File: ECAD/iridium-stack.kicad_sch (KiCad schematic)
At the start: 10 parts

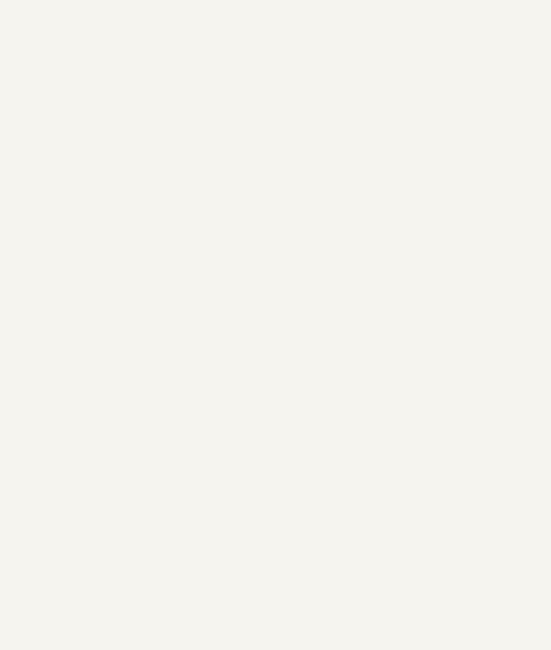
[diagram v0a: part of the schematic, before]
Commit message: finish symbol, update footprint
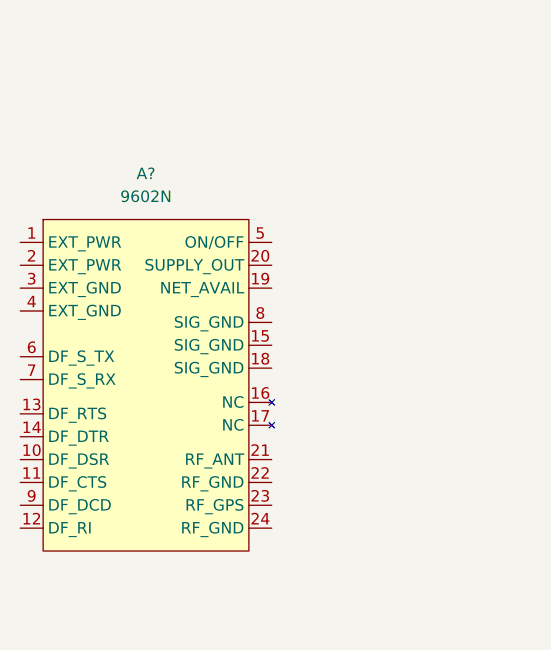
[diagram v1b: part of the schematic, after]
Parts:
- added A?: 9602N, symbol 9602N:9602N
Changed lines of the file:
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@@
     (pin "1")
+  )
+  (symbol (lib_id "9602N:9602N") (at 133.35 64.77 0) (unit 1)
+    (in_bom yes) (on_board yes) (fields_autoplaced)
+    (property "Reference" "A?" (id 0) (at 133.35 60.96 0))
+    (property "Value" "9602N" (id 1) (at 133.35 63.5 0))
+    (property "Footprint" "" (id 2) (at 133.35 64.77 0)
+      (effects (font (size 1.27 1.27)) hide)
+    )
+    (property "Datasheet" "" (id 3) (at 133.35 64.77 0)
+      (effects (font (size 1.27 1.27)) hide)
+    )
+    (pin "1")
+    (pin "10")
+    (pin "11")
+    (pin "12")
+    (pin "13")
+    (pin "14")
+    (pin "15")
+    (pin "16")
+    (pin "17")
+    (pin "18")
+    (pin "19")
+    (pin "2")
+    (pin "20")
+    (pin "21")
+    (pin "22")
+    (pin "23")
+    (pin "24")
+    (pin "3")
+    (pin "4")
+    (pin "5")
+    (pin "6")
+    (pin "7")
+    (pin "8")
+    (pin "9")
   )
   (sheet_instances
@@
       (reference "#PWR0112") (unit 1) (value "GND") (footprint "")
     )
+    (path "/4d3f3d34-821b-4ab9-8d48-8bbca7e30590"
+      (reference "A?") (unit 1) (value "9602N") (footprint "")
+    )
     (path "/00000000-0000-0000-0000-0000622296c8"

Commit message: power
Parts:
- added TH?: NTC, symbol Device:Thermistor_NTC
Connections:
- net +5V: now also TH?.2
- net GND: now also A?.3 (EXT_GND), A?.4 (EXT_GND)
- net +5VP: now reaches A?.1 (EXT_PWR)
- net +5VP: now also A?.2 (EXT_PWR), TH?.1
- net at A?.15 (SIG_GND): now also A?.18 (SIG_GND), A?.8 (SIG_GND)
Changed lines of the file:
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@@
   (junction (at 270.51 85.09) (diameter 0) (color 0 0 0 0)
   )
+  (junction (at 116.84 68.58) (diameter 0) (color 0 0 0 0)
+  )
+  (junction (at 116.84 76.2) (diameter 0) (color 0 0 0 0)
+  )
+  (junction (at 149.86 80.01) (diameter 0) (color 0 0 0 0)
+  )
+  (wire (pts (xy 147.32 77.47) (xy 149.86 77.47))
+    (stroke (width 0) (type default) (color 0 0 0 0))
+  )
   (wire (pts (xy 250.19 82.55) (xy 254 82.55))
     (stroke (width 0) (type default) (color 0 0 0 0))
   )
+  (wire (pts (xy 93.98 54.61) (xy 97.79 54.61))
+    (stroke (width 0) (type default) (color 0 0 0 0))
+  )
+  (wire (pts (xy 149.86 77.47) (xy 149.86 80.01))
+    (stroke (width 0) (type default) (color 0 0 0 0))
+  )
+  (wire (pts (xy 116.84 71.12) (xy 119.38 71.12))
+    (stroke (width 0) (type default) (color 0 0 0 0))
+  )
+  (wire (pts (xy 149.86 80.01) (xy 149.86 82.55))
+    (stroke (width 0) (type default) (color 0 0 0 0))
+  )
+  (wire (pts (xy 116.84 68.58) (xy 119.38 68.58))
+    (stroke (width 0) (type default) (color 0 0 0 0))
+  )
   (wire (pts (xy 270.51 85.09) (xy 266.7 85.09))
     (stroke (width 0) (type default) (color 0 0 0 0))
@@
     (stroke (width 0) (type default) (color 0 0 0 0))
   )
+  (wire (pts (xy 119.38 73.66) (xy 116.84 73.66))
+    (stroke (width 0) (type default) (color 0 0 0 0))
+  )
+  (wire (pts (xy 147.32 80.01) (xy 149.86 80.01))
+    (stroke (width 0) (type default) (color 0 0 0 0))
+  )
   (wire (pts (xy 266.7 82.55) (xy 270.51 82.55))
+    (stroke (width 0) (type default) (color 0 0 0 0))
+  )
+  (wire (pts (xy 116.84 68.58) (xy 116.84 71.12))
+    (stroke (width 0) (type default) (color 0 0 0 0))
+  )
+  (wire (pts (xy 116.84 73.66) (xy 116.84 76.2))
+    (stroke (width 0) (type default) (color 0 0 0 0))
+  )
+  (wire (pts (xy 149.86 82.55) (xy 147.32 82.55))
+    (stroke (width 0) (type default) (color 0 0 0 0))
+  )
+  (wire (pts (xy 116.84 76.2) (xy 119.38 76.2))
+    (stroke (width 0) (type default) (color 0 0 0 0))
+  )
+  (wire (pts (xy 82.55 54.61) (xy 86.36 54.61))
     (stroke (width 0) (type default) (color 0 0 0 0))
   )
@@
     (pin "1")
   )
+  (symbol (lib_id "power:GND") (at 116.84 76.2 0) (unit 1)
+    (in_bom yes) (on_board yes)
+    (property "Reference" "#PWR?" (id 0) (at 116.84 82.55 0)
+      (effects (font (size 1.27 1.27)) hide)
+    )
+    (property "Value" "GND" (id 1) (at 116.84 80.01 0))
+    (property "Footprint" "" (id 2) (at 116.84 76.2 0)
+      (effects (font (size 1.27 1.27)) hide)
+    )
+    (property "Datasheet" "" (id 3) (at 116.84 76.2 0)
+      (effects (font (size 1.27 1.27)) hide)
+    )
+    (pin "1")
+  )
   (symbol (lib_id "9602N:9602N") (at 133.35 64.77 0) (unit 1)
     (in_bom yes) (on_board yes) (fields_autoplaced)
@@
     (pin "9")
   )
+  (symbol (lib_id "Device:Thermistor_NTC") (at 90.17 54.61 270) (unit 1)
+    (in_bom yes) (on_board yes)
+    (property "Reference" "TH?" (id 0) (at 90.17 48.26 90))
+    (property "Value" "NTC" (id 1) (at 90.17 50.8 90))
+    (property "Footprint" "" (id 2) (at 91.44 54.61 0)
+      (effects (font (size 1.27 1.27)) hide)
+    )
+    (property "Datasheet" "~" (id 3) (at 91.44 54.61 0)
+      (effects (font (size 1.27 1.27)) hide)
+    )
+    (pin "1")
+    (pin "2")
+  )
+  (symbol (lib_id "power:+5VP") (at 116.84 68.58 0) (unit 1)
+    (in_bom yes) (on_board yes) (fields_autoplaced)
+    (property "Reference" "#PWR?" (id 0) (at 116.84 72.39 0)
+      (effects (font (size 1.27 1.27)) hide)
+    )
+    (property "Value" "+5VP" (id 1) (at 116.84 63.5 0))
+    (property "Footprint" "" (id 2) (at 116.84 68.58 0)
+      (effects (font (size 1.27 1.27)) hide)
+    )
+    (property "Datasheet" "" (id 3) (at 116.84 68.58 0)
+      (effects (font (size 1.27 1.27)) hide)
+    )
+    (pin "1")
+  )
+  (symbol (lib_id "power:+5V") (at 82.55 54.61 0) (unit 1)
+    (in_bom yes) (on_board yes) (fields_autoplaced)
+    (property "Reference" "#PWR?" (id 0) (at 82.55 58.42 0)
+      (effects (font (size 1.27 1.27)) hide)
+    )
+    (property "Value" "+5V" (id 1) (at 82.55 49.53 0))
+    (property "Footprint" "" (id 2) (at 82.55 54.61 0)
+      (effects (font (size 1.27 1.27)) hide)
+    )
+    (property "Datasheet" "" (id 3) (at 82.55 54.61 0)
+      (effects (font (size 1.27 1.27)) hide)
+    )
+    (pin "1")
+  )
+  (symbol (lib_id "power:+5VP") (at 97.79 54.61 0) (unit 1)
+    (in_bom yes) (on_board yes) (fields_autoplaced)
+    (property "Reference" "#PWR?" (id 0) (at 97.79 58.42 0)
+      (effects (font (size 1.27 1.27)) hide)
+    )
+    (property "Value" "+5VP" (id 1) (at 97.79 49.53 0))
+    (property "Footprint" "" (id 2) (at 97.79 54.61 0)
+      (effects (font (size 1.27 1.27)) hide)
+    )
+    (property "Datasheet" "" (id 3) (at 97.79 54.61 0)
+      (effects (font (size 1.27 1.27)) hide)
+    )
+    (pin "1")
+  )
   (sheet_instances
     (path "/" (page "1"))
@@
       (reference "#PWR0112") (unit 1) (value "GND") (footprint "")
     )
+    (path "/243ec770-cc5a-4509-9c36-eb8c7bb8645d"
+      (reference "#PWR?") (unit 1) (value "GND") (footprint "")
+    )
+    (path "/bf8825e1-0059-4b49-b8f9-cbb3bb661ba2"
+      (reference "#PWR?") (unit 1) (value "+5VP") (footprint "")
+    )
+    (path "/dd479a80-227b-44d6-b0fa-58cd4309c382"
+      (reference "#PWR?") (unit 1) (value "+5V") (footprint "")
+    )
+    (path "/e45ee289-0e09-4fb1-8e60-b9936eece8bf"
+      (reference "#PWR?") (unit 1) (value "+5VP") (footprint "")
+    )
     (path "/4d3f3d34-821b-4ab9-8d48-8bbca7e30590"
       (reference "A?") (unit 1) (value "9602N") (footprint "")
@@
       (reference "MH4") (unit 1) (value "M3") (footprint "MountingHole:MountingHole_3.2mm_M3_Pad")
     )
-  )
+    (path "/b31ebd25-cf4c-4c3e-b83d-0ec793b65cd9"
+      (reference "TH?") (unit 1) (value "NTC") (footprint "")
+    )
+  )

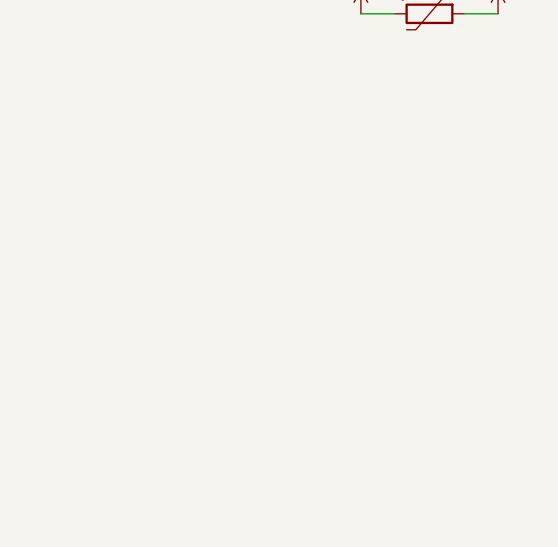
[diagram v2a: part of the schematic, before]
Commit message: add synchronous buck
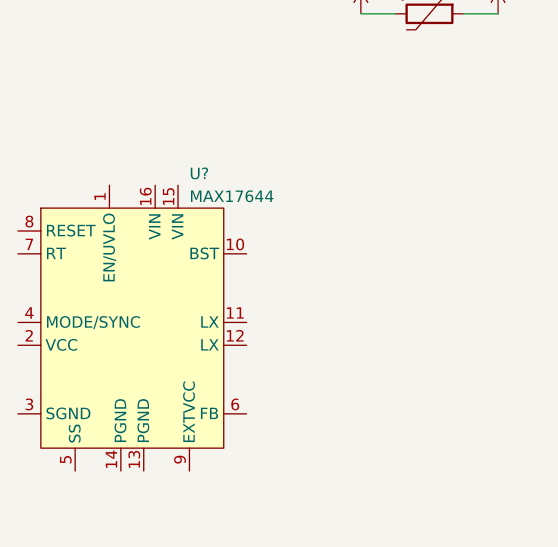
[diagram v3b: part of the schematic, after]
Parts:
- added U?: MAX17644, symbol Symbols:MAX17644
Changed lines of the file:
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@@
     (pin "1")
+  )
+  (symbol (lib_id "Symbols:MAX17644") (at 57.15 71.12 0) (unit 1)
+    (in_bom yes) (on_board yes)
+    (property "Reference" "U?" (id 0) (at 63.5 72.39 0)
+      (effects (font (size 1.27 1.27)) (justify left))
+    )
+    (property "Value" "MAX17644" (id 1) (at 63.5 74.93 0)
+      (effects (font (size 1.27 1.27)) (justify left))
+    )
+    (property "Footprint" "" (id 2) (at 57.15 71.12 0)
+      (effects (font (size 1.27 1.27)) hide)
+    )
+    (property "Datasheet" "" (id 3) (at 57.15 71.12 0)
+      (effects (font (size 1.27 1.27)) hide)
+    )
+    (pin "1")
+    (pin "10")
+    (pin "11")
+    (pin "12")
+    (pin "13")
+    (pin "14")
+    (pin "15")
+    (pin "16")
+    (pin "2")
+    (pin "3")
+    (pin "4")
+    (pin "5")
+    (pin "6")
+    (pin "7")
+    (pin "8")
+    (pin "9")
   )
   (symbol (lib_id "power:GND") (at 116.84 76.2 0) (unit 1)
@@
       (reference "TH?") (unit 1) (value "NTC") (footprint "")
     )
-  )
+    (path "/02a9969f-ce81-4a97-8ae7-0a755196af14"
+      (reference "U?") (unit 1) (value "MAX17644") (footprint "")
+    )
+  )

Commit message: ap62301
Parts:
- removed U?: MAX17644, symbol Symbols:MAX17644
- added C?: 0.1uF, symbol Device:C
- added C?: C, symbol Device:C
- added L?: L, symbol Device:L
- added R? (x2): R, symbol Device:R
- added R?: 3K, symbol Device:R
- added R?: 12.5K, symbol Device:R
- added U?: AP62301WU-7, symbol Symbols:AP62301WU-7
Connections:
- new net: R?.1, R?.2, U?.6 (FB)
- new net: C?.2, R?.2, R?.2, U?.3 (GND)
- new net: C?.1, U?.4 (BST)
- new net: C?.2, L?.1, U?.2 (SW)
- new net: C?.1, R?.1, U?.1 (VIN)
- new net: R?.1, R?.2, U?.5 (EN)
- new net: L?.2, R?.1
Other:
- note added: "6.2V UVLO"
- note added: "Synchronous Buck - Stable 5V"

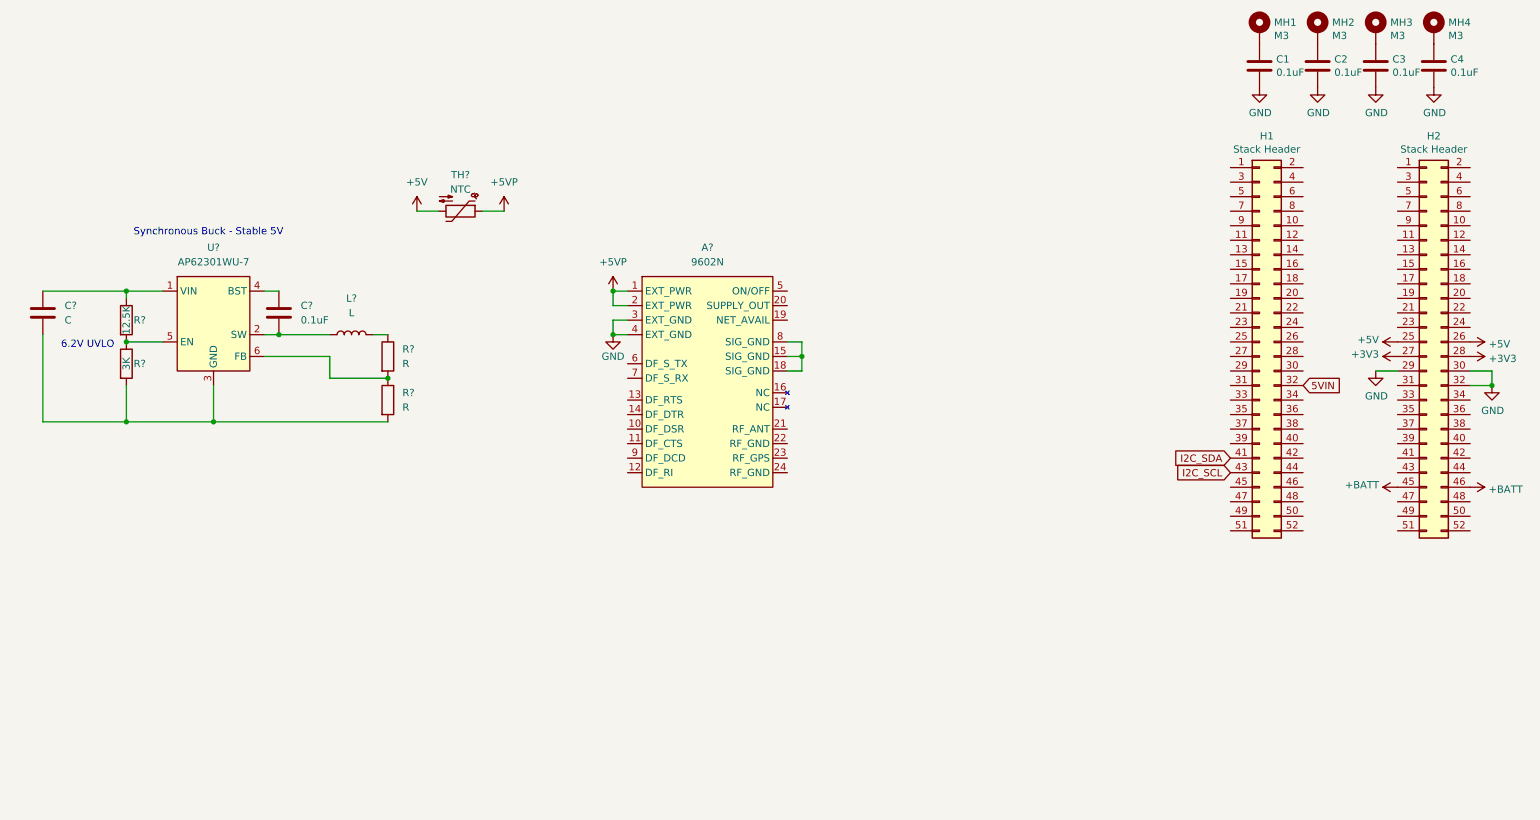
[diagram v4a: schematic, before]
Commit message: Add buck and more nets
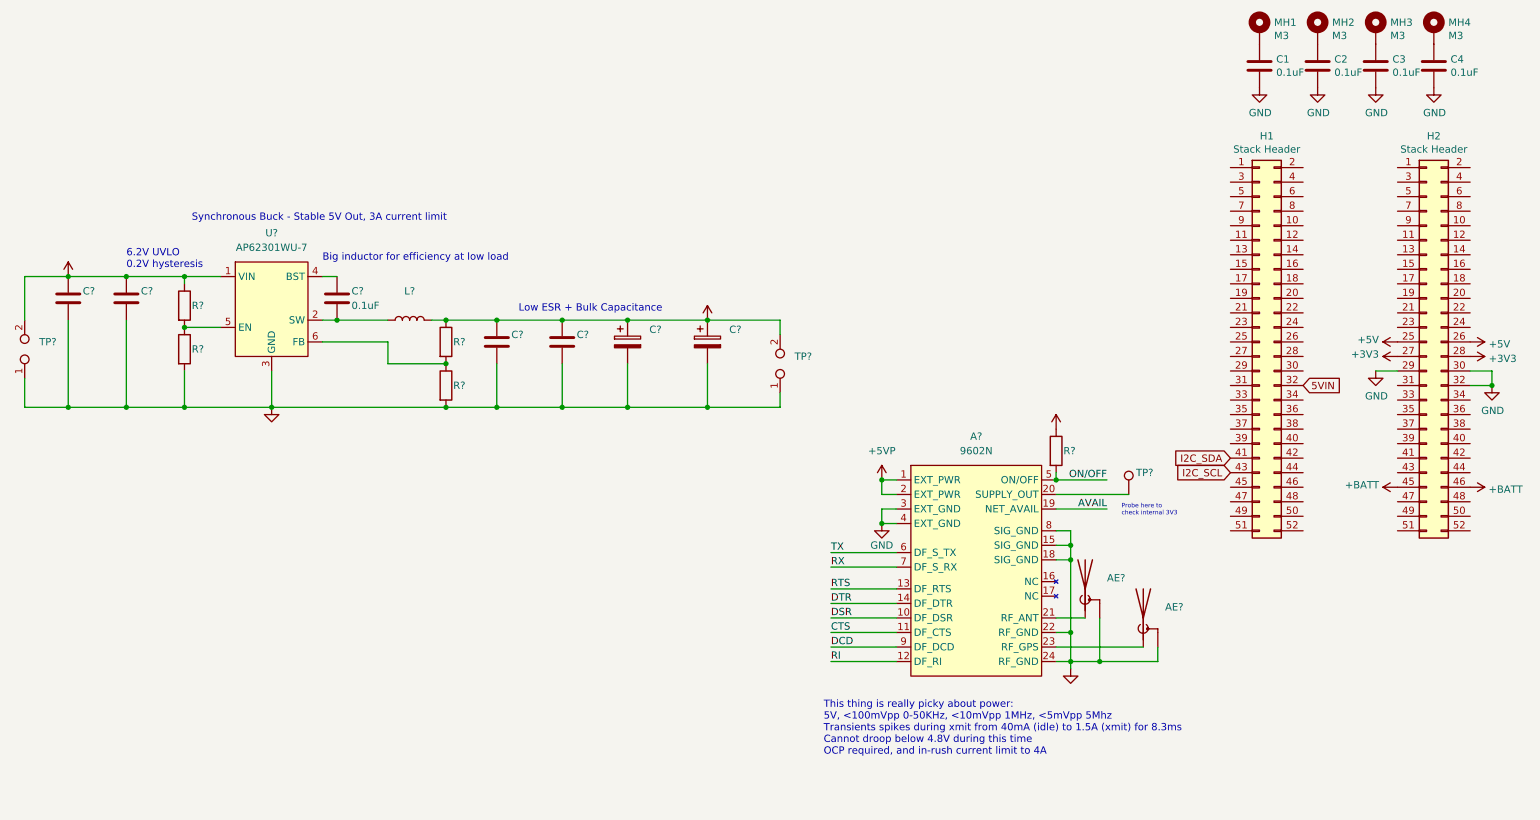
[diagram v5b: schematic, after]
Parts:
- removed TH?: NTC, symbol Device:Thermistor_NTC
- added AE? (x2): (no value), symbol Device:Antenna_Shield
- added C? (x2): (no value), symbol Device:C_Polarized
- added C? (x3): (no value), symbol Device:C
- added R?: (no value), symbol Device:R
- added TP? (x2): (no value), symbol Connector:TestPoint_2Pole
- added TP?: (no value), symbol Connector:TestPoint
- C?: value C -> (none)
- L?: value L -> (none)
- R? (x2): value R -> (none)
- R?: value 3K -> (none)
- R?: value 12.5K -> (none)
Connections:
- net +5VP: now also L?.2, R?.1, C?.1, C?.1, C?.1, C?.1, R?.1, TP?.2
- net +BATT: now also C?.1, R?.1, U?.1 (VIN), C?.1, TP?.2
- net GND: now also A?.15 (SIG_GND), A?.18 (SIG_GND), A?.22 (RF_GND), A?.24 (RF_GND), A?.8 (SIG_GND), C?.2, R?.2, R?.2, U?.3 (GND), AE?.2 (Shield), AE?.2 (Shield), C?.2, C?.2, C?.2, C?.2, C?.2, TP?.1, TP?.1
- net DSR: now reaches A?.10 (DF_DSR)
- net CTS: now reaches A?.11 (DF_CTS)
- net RI: now reaches A?.12 (DF_RI)
- net RTS: now reaches A?.13 (DF_RTS)
- net DTR: now reaches A?.14 (DF_DTR)
- net AVAIL: now reaches A?.19 (NET_AVAIL)
- net at A?.20 (SUPPLY_OUT): now also TP?.1
- net at A?.21 (RF_ANT): now also AE?.1 (A)
- net at A?.23 (RF_GPS): now also AE?.1 (A)
- net ON/OFF: now reaches A?.5 (ON/OFF)
- net ON/OFF: now also R?.2
- net TX: now reaches A?.6 (DF_S_TX)
- net RX: now reaches A?.7 (DF_S_RX)
- net DCD: now reaches A?.9 (DF_DCD)
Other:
- note added: "6.2V UVLO 0.2V hysteresis"
- note added: "Big inductor for efficiency at low load"
- note added: "Low ESR + Bulk Capacitance"
- note added: "Probe here to check internal 3V3"
- note added: "Synchronous Buck - Stable 5V Out, 3A current limit"
- note added: "This thing is really picky about power: 5V, <100mVpp 0-50KHz, <10mVpp 1MHz, <5mVpp 5Mhz Transients spikes during xmit from 40mA (idle) to 1.5A (xmit) for 8.3ms Cannot droop below 4.8V during this time OCP required, and in-rush current limit to 4A"
- note removed: "6.2V UVLO"
- note removed: "Synchronous Buck - Stable 5V"
- moved on the sheet: A?, C?, L?, R?, U?

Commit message: revise on/off circuit
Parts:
- added Q?: 2N7002, Package_TO_SOT_SMD:SOT-23, symbol Transistor_FET:2N7002
- AE? (x2): value (none) -> Coax
- C? (x2): value (none) -> 100uF
- C? (x2): value (none) -> 47uF
- C? (x2): value (none) -> 10uF
- L?: value (none) -> 33uH
- R?: value (none) -> 10K
- R?: value (none) -> 100K
- R?: value (none) -> 118K
- R?: value (none) -> 59K
- R?: value (none) -> 52.3K
- TP?: value (none) -> VBAT
- TP?: value (none) -> VSUP
- TP?: value (none) -> 5V_Protected
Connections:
- net GND: now also Q?.2 (S)
- net ON/OFF: now also Q?.1 (G); no longer A?.5 (ON/OFF), R?.2
- net at R?.1, R?.2, U?.5 (EN): now also Q?.3 (D)
- new net: A?.5 (ON/OFF), R?.2
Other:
- moved on the sheet: TP?

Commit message: finished v1
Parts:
- removed AE?: Coax, symbol Device:Antenna_Shield
- removed R?: 100K, symbol Device:R
- added C?: 100uF, symbol Device:C_Polarized
- added J?: Header, symbol Connector:Conn_01x12_Male
- L?: value 33uH -> 10uH
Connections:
- net +5VP: now also A?.5 (ON/OFF), C?.1
- net +BATT: now also J?.1 (Pin_1)
- net AVAIL: now also J?.12 (Pin_12)
- net CTS: now also J?.9 (Pin_9)
- net DCD: now also J?.10 (Pin_10)
- net DSR: now also J?.8 (Pin_8)
- net DTR: now also J?.7 (Pin_7)
- net GND: now also C?.2, J?.2 (Pin_2); no longer A?.24 (RF_GND)
- net ON/OFF: now also J?.3 (Pin_3)
- net RI: now also J?.11 (Pin_11)
- net RTS: now also J?.6 (Pin_6)
- net RX: now also J?.5 (Pin_5)
- net TX: now also J?.4 (Pin_4)
- no-connect marks 0 -> 2
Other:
- note added: "18V MAX input"
- note added: "All logic is 3.3V logic level, but is 5V tolerant TX and RX are from master device (TX is input to the 9602, RX is output from the 9602)"
- note added: "ESR primarily determines output ripple - see datasheet"
- note added: "Inductor is balance between transient response and efficiency at low-load"
- note added: "Low ESR MLCC + Tantalum Bulk Capacitance"
- note removed: "Big inductor for efficiency at low load"
- note removed: "Low ESR + Bulk Capacitance"
- moved on the sheet: TP?
